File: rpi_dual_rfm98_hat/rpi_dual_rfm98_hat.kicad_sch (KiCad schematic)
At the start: 12 parts, among them J1 PJ-202A, P1 Conn_02x20_Odd_Even, SW1 SW_Push_Open_Dual, U1 E32400M30S, U2 OLED

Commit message: ready for review
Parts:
- removed J1: PJ-202A, PJ-202A:CUI_PJ-202A, symbol PJ-202A:PJ-202A
- removed R1, R2: 1k, Resistor_SMD:R_1206_3216Metric_Pad1.30x1.75mm_HandSolder, symbol Device:R
- removed R3: 10k, Resistor_SMD:R_1206_3216Metric_Pad1.30x1.75mm_HandSolder, symbol Device:R
- removed SW1: SW_Push_Open_Dual, Button_Switch_SMD:SW_Push_1P1T_NO_6x6mm_H9.5mm, symbol Switch:SW_Push_Open_Dual
- removed U1: E32400M30S, TinyGS:E32400M, symbol TinyGS:E32400M30S
- removed U2: OLED, TinyGS:OLED, symbol TinyGS:OLED
- added D1, D2, D3: LED, LED_SMD:LED_0603_1608Metric, symbol Device:LED
- added J1: Conn_01x02_Male, Connector_JST:JST_XH_B2B-XH-AM_1x02_P2.50mm_Vertical, symbol Connector:Conn_01x02_Male
- added J2, J3: Conn_Coaxial, Connector_Coaxial:SMA_Amphenol_132134-11_Vertical, symbol Connector:Conn_Coaxial
- added J4: Conn_01x03_Male, Connector_JST:JST_XH_B3B-XH-AM_1x03_P2.50mm_Vertical, symbol Connector:Conn_01x03_Male
- added R1, R2, R3: R_US, Resistor_SMD:R_0603_1608Metric, symbol Device:R_US
- added U1, U2: RFM98PW-symbols, mainboard:RFM95PW, symbol mainboard:RFM98PW-symbols
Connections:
- net +5V: now also D1.2 (A), J1.1 (Pin_1), U1.5 (VCC), U2.5 (VCC)
- net GND: now also J1.2 (Pin_2), J2.2 (Ext), J3.2 (Ext), J4.3 (Pin_3), R1.2, R2.2, R3.2, U1.16 (GND), U1.17 (GND), U1.2 (GND), U2.16 (GND), U2.17 (GND), U2.2 (GND)
- net GPIO10(SPI0_MOSI): now also U1.11 (MOSI)
- net GPIO11(SPI0_SCK): now also U1.12 (SCK)
- net GPIO17(GEN0): now also D3.2 (A)
- net GPIO19(SPI1_MISO): now also U2.10 (MISO)
- net GPIO20(SPI1_MOSI): now also U2.11 (MOSI)
- net GPIO21(SPI1_SCK): now also U2.12 (SCK)
- net GPIO22(GEN3): now also U2.6 (GPIO_0)
- net GPIO23(GEN4): now also U1.6 (GPIO_0)
- net GPIO24(GEN5): now also U2.14 (RESET)
- net GPIO25(GEN6): now also U1.14 (RESET)
- net GPIO26: now also J4.1 (Pin_1), J4.2 (Pin_2)
- net GPIO27(GEN2): now also D2.2 (A)
- net GPIO7(SPI1_CE_N): now also U2.13 (NSS)
- net GPIO8(SPI0_CE_N): now also U1.13 (NSS)
- net GPIO9(SPI0_MISO): now also U1.10 (MISO)
- net +3V3: no longer names the net of P1.1 (Pin_1)
- net +3V3: no longer P1.17 (Pin_17)
- new net: D1.1 (K), R1.1
- new net: D3.1 (K), R3.1
- new net: J2.1 (In), U1.1 (ANT)
- new net: J3.1 (In), U2.1 (ANT)
- new net: D2.1 (K), R2.1
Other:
- note added: "Power"
- note added: "RX Radio"
- note added: "RX/TX Switch"
- note added: "Raspberry Pi"
- note added: "TX Radio"
- moved on the sheet: P1

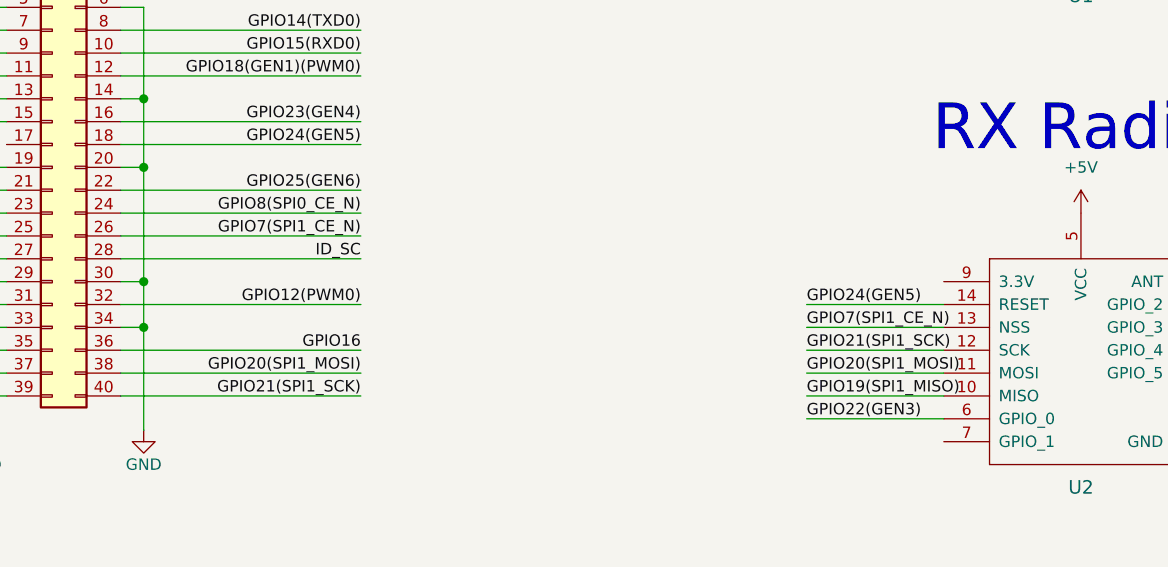
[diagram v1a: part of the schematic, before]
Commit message: Re-mapped SPI1 CE pin
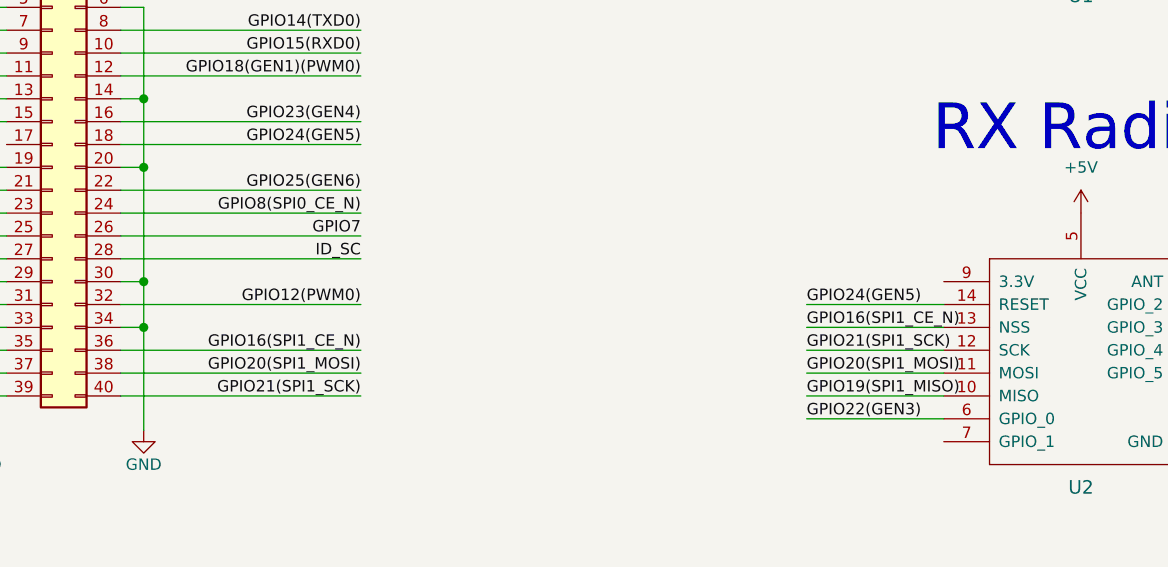
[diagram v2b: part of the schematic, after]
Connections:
- net GPIO16 renamed GPIO16(SPI1_CE_N)
- net GPIO16(SPI1_CE_N): now also U2.13 (NSS)
- net GPIO7(SPI1_CE_N) renamed GPIO7
- net GPIO7: no longer U2.13 (NSS)
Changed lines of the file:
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@@
     (effects (font (size 1.27 1.27)) (justify left bottom))
   )
-  (label "GPIO7(SPI1_CE_N)" (at 95.25 127 180)
+  (label "GPIO7" (at 95.25 127 180)
     (effects (font (size 1.27 1.27)) (justify right bottom))
   )
@@
     (effects (font (size 1.27 1.27)) (justify left bottom))
   )
-  (label "GPIO16" (at 95.25 139.7 180)
+  (label "GPIO16(SPI1_CE_N)" (at 95.25 139.7 180)
     (effects (font (size 1.27 1.27)) (justify right bottom))
   )
@@
     (effects (font (size 1.27 1.27)) (justify left bottom))
   )
-  (label "GPIO7(SPI1_CE_N)" (at 144.78 137.16 0)
+  (label "GPIO16(SPI1_CE_N)" (at 144.78 137.16 0)
     (effects (font (size 1.27 1.27)) (justify left bottom))
   )

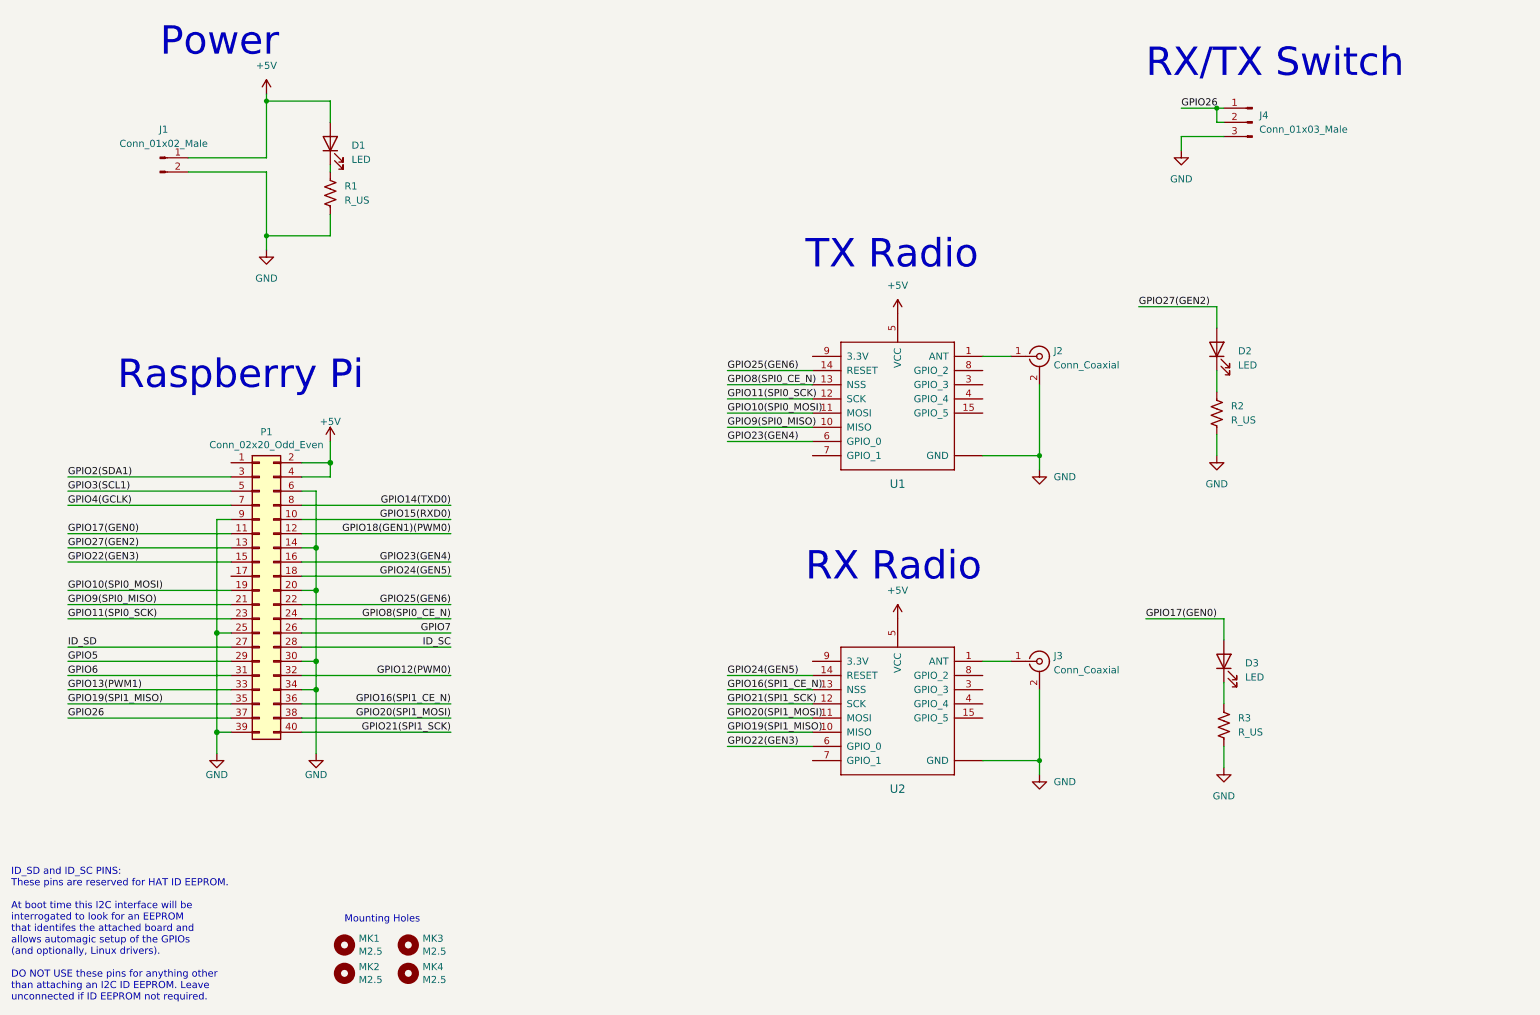
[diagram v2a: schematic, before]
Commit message: add CS pullups, ground under antenna connectors
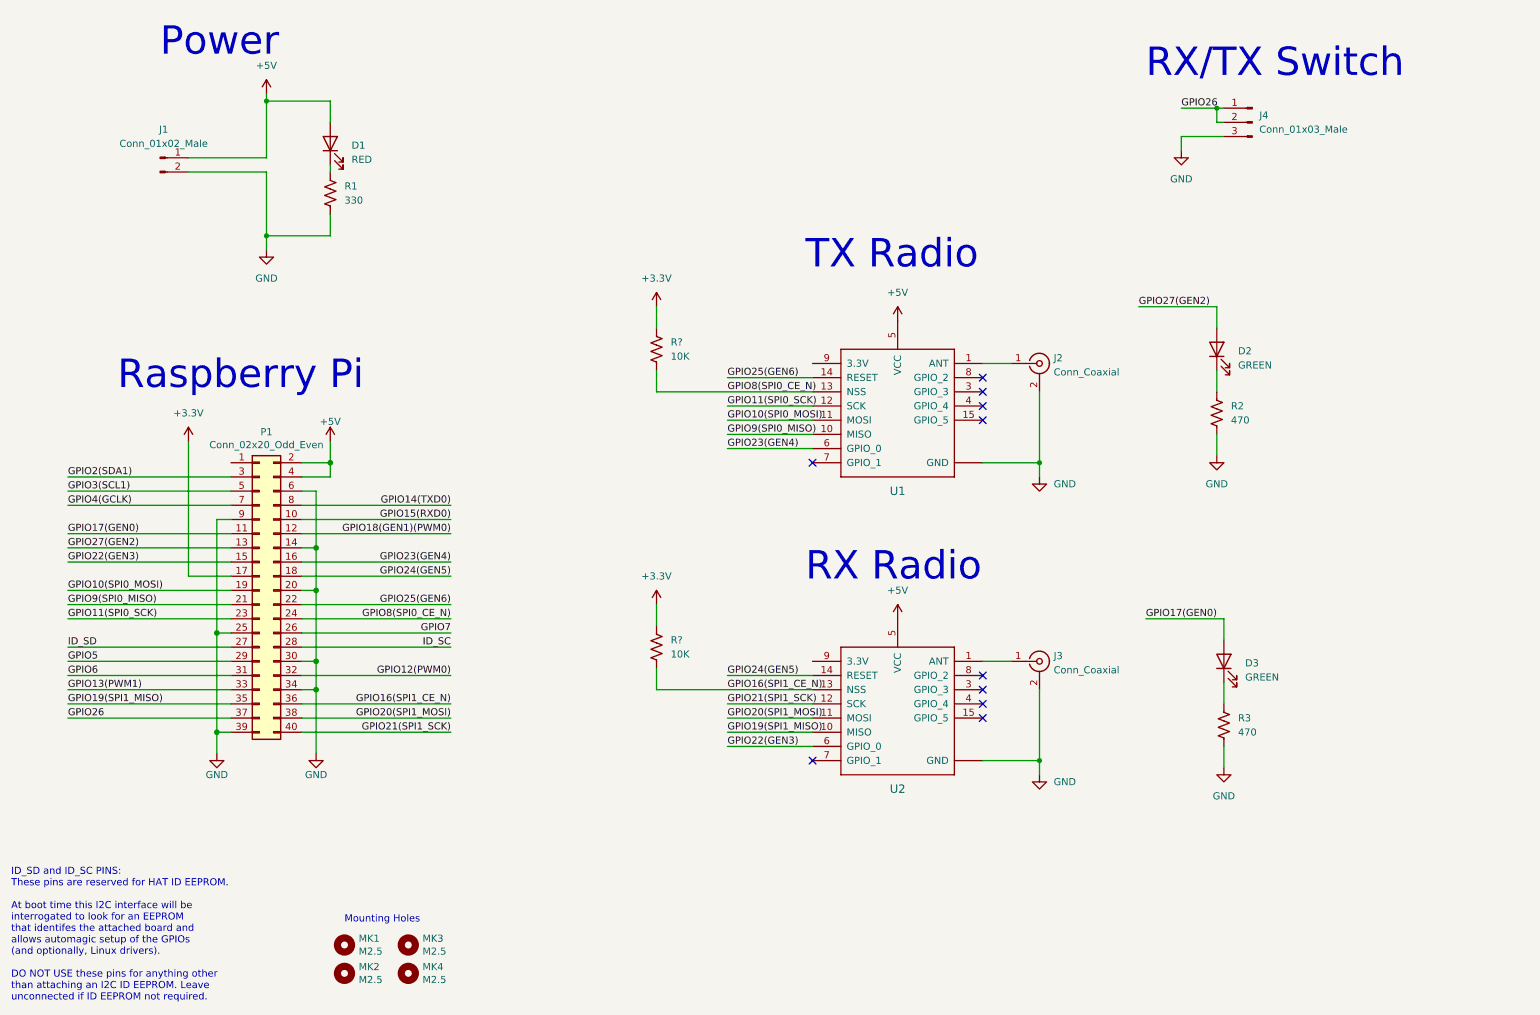
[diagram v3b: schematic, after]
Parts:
- added R? (x2): 10K, Resistor_SMD:R_0603_1608Metric, symbol Device:R_US
- D1: value LED -> RED
- D2, D3: value LED -> GREEN
- R1: value R_US -> 330
- R2, R3: value R_US -> 470
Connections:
- net GPIO16(SPI1_CE_N): now also R?.2
- net GPIO8(SPI0_CE_N): now also R?.2
- net +3V3: now reaches P1.17 (Pin_17)
- net +3V3: now also R?.1, R?.1
- no-connect marks 0 -> 10
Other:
- moved on the sheet: J2, U1

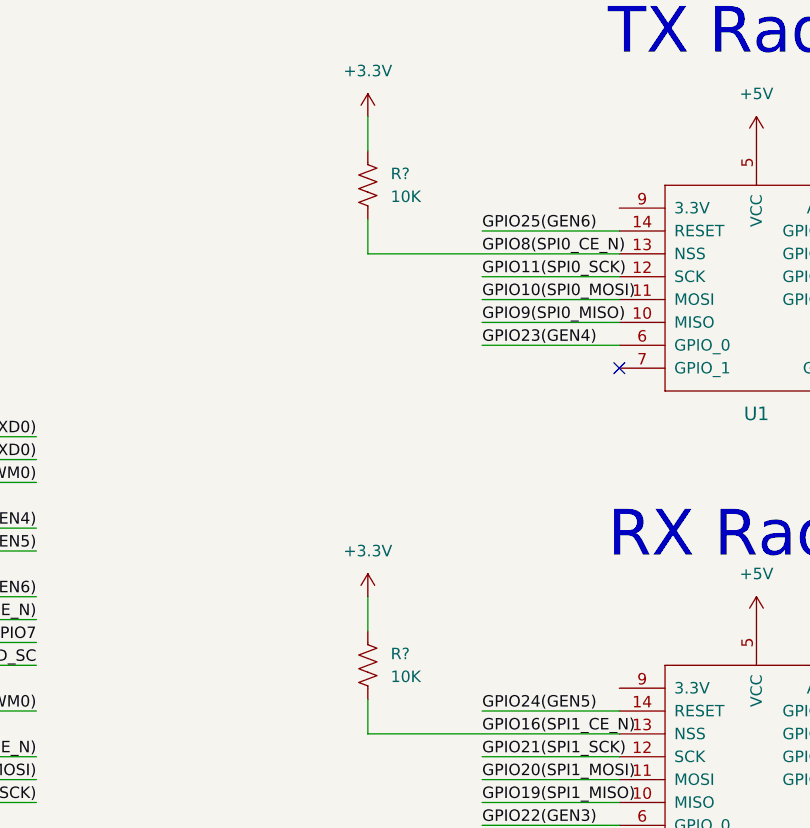
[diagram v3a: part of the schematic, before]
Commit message: schematic changes aligning with previous commit
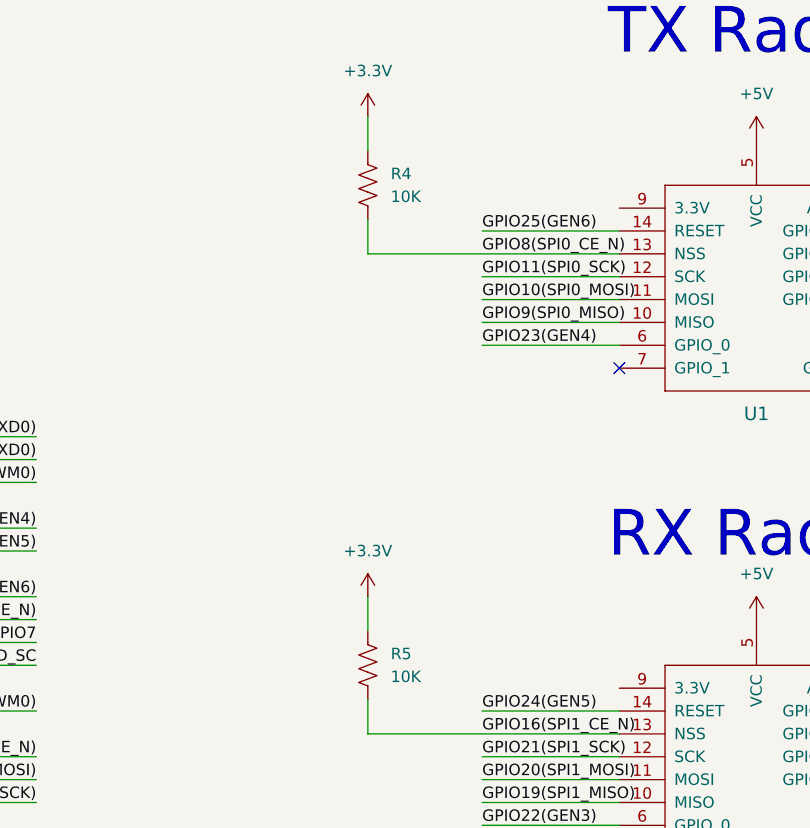
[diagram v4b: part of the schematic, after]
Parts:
- gave numbers to parts that had none: 2
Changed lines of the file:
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@@
   (symbol (lib_id "power:+3.3V") (at 48.26 92.71 0) (unit 1)
     (in_bom yes) (on_board yes) (fields_autoplaced)
-    (property "Reference" "#PWR?" (id 0) (at 48.26 96.52 0)
+    (property "Reference" "#PWR0101" (id 0) (at 48.26 96.52 0)
       (effects (font (size 1.27 1.27)) hide)
     )
@@
   (symbol (lib_id "power:+3.3V") (at 132.08 68.58 0) (unit 1)
     (in_bom yes) (on_board yes) (fields_autoplaced)
-    (property "Reference" "#PWR?" (id 0) (at 132.08 72.39 0)
+    (property "Reference" "#PWR0102" (id 0) (at 132.08 72.39 0)
       (effects (font (size 1.27 1.27)) hide)
     )
@@
   (symbol (lib_id "Device:R_US") (at 132.08 129.54 0) (unit 1)
     (in_bom yes) (on_board yes) (fields_autoplaced)
-    (property "Reference" "R?" (id 0) (at 134.62 128.2699 0)
+    (property "Reference" "R5" (id 0) (at 134.62 128.2699 0)
       (effects (font (size 1.27 1.27)) (justify left))
     )
@@
   (symbol (lib_id "power:+3.3V") (at 132.08 121.92 0) (unit 1)
     (in_bom yes) (on_board yes) (fields_autoplaced)
-    (property "Reference" "#PWR?" (id 0) (at 132.08 125.73 0)
+    (property "Reference" "#PWR0103" (id 0) (at 132.08 125.73 0)
       (effects (font (size 1.27 1.27)) hide)
     )
@@
   (symbol (lib_id "Device:R_US") (at 132.08 76.2 0) (unit 1)
     (in_bom yes) (on_board yes) (fields_autoplaced)
-    (property "Reference" "R?" (id 0) (at 134.62 74.9299 0)
+    (property "Reference" "R4" (id 0) (at 134.62 74.9299 0)
       (effects (font (size 1.27 1.27)) (justify left))
     )
@@
     )
     (path "/a2fd471d-3e12-476d-a5a0-90a04dca364c"
-      (reference "#PWR?") (unit 1) (value "+3.3V") (footprint "")
+      (reference "#PWR0101") (unit 1) (value "+3.3V") (footprint "")
     )
     (path "/b9407fe6-f1cf-4825-8663-0abf7fd1f2f5"
-      (reference "#PWR?") (unit 1) (value "+3.3V") (footprint "")
+      (reference "#PWR0102") (unit 1) (value "+3.3V") (footprint "")
     )
     (path "/d7c8303f-5b99-4f7e-8c15-deab02a60d2a"
-      (reference "#PWR?") (unit 1) (value "+3.3V") (footprint "")
+      (reference "#PWR0103") (unit 1) (value "+3.3V") (footprint "")
     )
     (path "/883a0fc5-3b19-49ad-9afb-f61d2e7f228f"
@@
       (reference "R3") (unit 1) (value "470") (footprint "Resistor_SMD:R_0603_1608Metric")
     )
+    (path "/d9d23d87-3a7b-404f-958e-588b0293f018"
+      (reference "R4") (unit 1) (value "10K") (footprint "Resistor_SMD:R_0603_1608Metric")
+    )
     (path "/d78b5a65-1fde-4ebc-9dc2-78efbddd07eb"
-      (reference "R?") (unit 1) (value "10K") (footprint "Resistor_SMD:R_0603_1608Metric")
-    )
-    (path "/d9d23d87-3a7b-404f-958e-588b0293f018"
-      (reference "R?") (unit 1) (value "10K") (footprint "Resistor_SMD:R_0603_1608Metric")
+      (reference "R5") (unit 1) (value "10K") (footprint "Resistor_SMD:R_0603_1608Metric")
     )
     (path "/bb120769-0ef8-4334-bd86-00b5e1753f3f"
